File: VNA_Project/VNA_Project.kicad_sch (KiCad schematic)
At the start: 0 parts

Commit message: Started on MCU design, for sweeping
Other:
- added sheet ADC (ADC.kicad_sch)
- added sheet DAC (DAC.kicad_sch)
- added sheet Directional Coupler (Directional_Coupler.kicad_sch)
- added sheet MCU (MCU_vna.kicad_sch)
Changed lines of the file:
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@@
+	)
+	(sheet
+		(at 157.48 38.1)
+		(size 27.94 26.67)
+		(exclude_from_sim no)
+		(in_bom yes)
+		(on_board yes)
+		(dnp no)
+		(fields_autoplaced yes)
+		(stroke
+			(width 0.1524)
+			(type solid)
+		)
+		(fill
+			(color 0 0 0 0.0000)
+		)
+		(property "Sheetname" "Directional Coupler"
+			(at 157.48 37.3884 0)
+			(effects
+				(font
+					(size 1.27 1.27)
+				)
+				(justify left bottom)
+			)
+		)
+		(property "Sheetfile" "Directional_Coupler.kicad_sch"
+			(at 157.48 65.3546 0)
+			(effects
+				(font
+					(size 1.27 1.27)
+				)
+				(justify left top)
+			)
+		)
+		(instances
+			(project "VNA_Project"
+				(path "/8b9c6944-c5f7-4a92-a452-dc4fa5f3924d"
+					(page "5")
+				)
+			)
+		)
+	)
+	(sheet
+		(at 115.57 38.1)
+		(size 26.67 26.67)
+		(exclude_from_sim no)
+		(in_bom yes)
+		(on_board yes)
+		(dnp no)
+		(fields_autoplaced yes)
+		(stroke
+			(width 0.1524)
+			(type solid)
+		)
+		(fill
+			(color 0 0 0 0.0000)
+		)
+		(property "Sheetname" "MCU"
+			(at 115.57 37.3884 0)
+			(effects
+				(font
+					(size 1.27 1.27)
+				)
+				(justify left bottom)
+			)
+		)
+		(property "Sheetfile" "MCU_vna.kicad_sch"
+			(at 115.57 65.3546 0)
+			(effects
+				(font
+					(size 1.27 1.27)
+				)
+				(justify left top)
+			)
+		)
+		(instances
+			(project "VNA_Project"
+				(path "/8b9c6944-c5f7-4a92-a452-dc4fa5f3924d"
+					(page "4")
+				)
+			)
+		)
+	)
+	(sheet
+		(at 76.2 76.2)
+		(size 26.67 22.86)
+		(exclude_from_sim no)
+		(in_bom yes)
+		(on_board yes)
+		(dnp no)
+		(fields_autoplaced yes)
+		(stroke
+			(width 0.1524)
+			(type solid)
+		)
+		(fill
+			(color 0 0 0 0.0000)
+		)
+		(property "Sheetname" "DAC"
+			(at 76.2 75.4884 0)
+			(effects
+				(font
+					(size 1.27 1.27)
+				)
+				(justify left bottom)
+			)
+		)
+		(property "Sheetfile" "DAC.kicad_sch"
+			(at 76.2 99.6446 0)
+			(effects
+				(font
+					(size 1.27 1.27)
+				)
+				(justify left top)
+			)
+		)
+		(instances
+			(project "VNA_Project"
+				(path "/8b9c6944-c5f7-4a92-a452-dc4fa5f3924d"
+					(page "7")
+				)
+			)
+		)
+	)
+	(sheet
+		(at 38.1 77.47)
+		(size 25.4 22.86)
+		(exclude_from_sim no)
+		(in_bom yes)
+		(on_board yes)
+		(dnp no)
+		(fields_autoplaced yes)
+		(stroke
+			(width 0.1524)
+			(type solid)
+		)
+		(fill
+			(color 0 0 0 0.0000)
+		)
+		(property "Sheetname" "ADC"
+			(at 38.1 76.7584 0)
+			(effects
+				(font
+					(size 1.27 1.27)
+				)
+				(justify left bottom)
+			)
+		)
+		(property "Sheetfile" "ADC.kicad_sch"
+			(at 38.1 100.9146 0)
+			(effects
+				(font
+					(size 1.27 1.27)
+				)
+				(justify left top)
+			)
+		)
+		(instances
+			(project "VNA_Project"
+				(path "/8b9c6944-c5f7-4a92-a452-dc4fa5f3924d"
+					(page "6")
+				)
+			)
+		)
 	)
 	(sheet

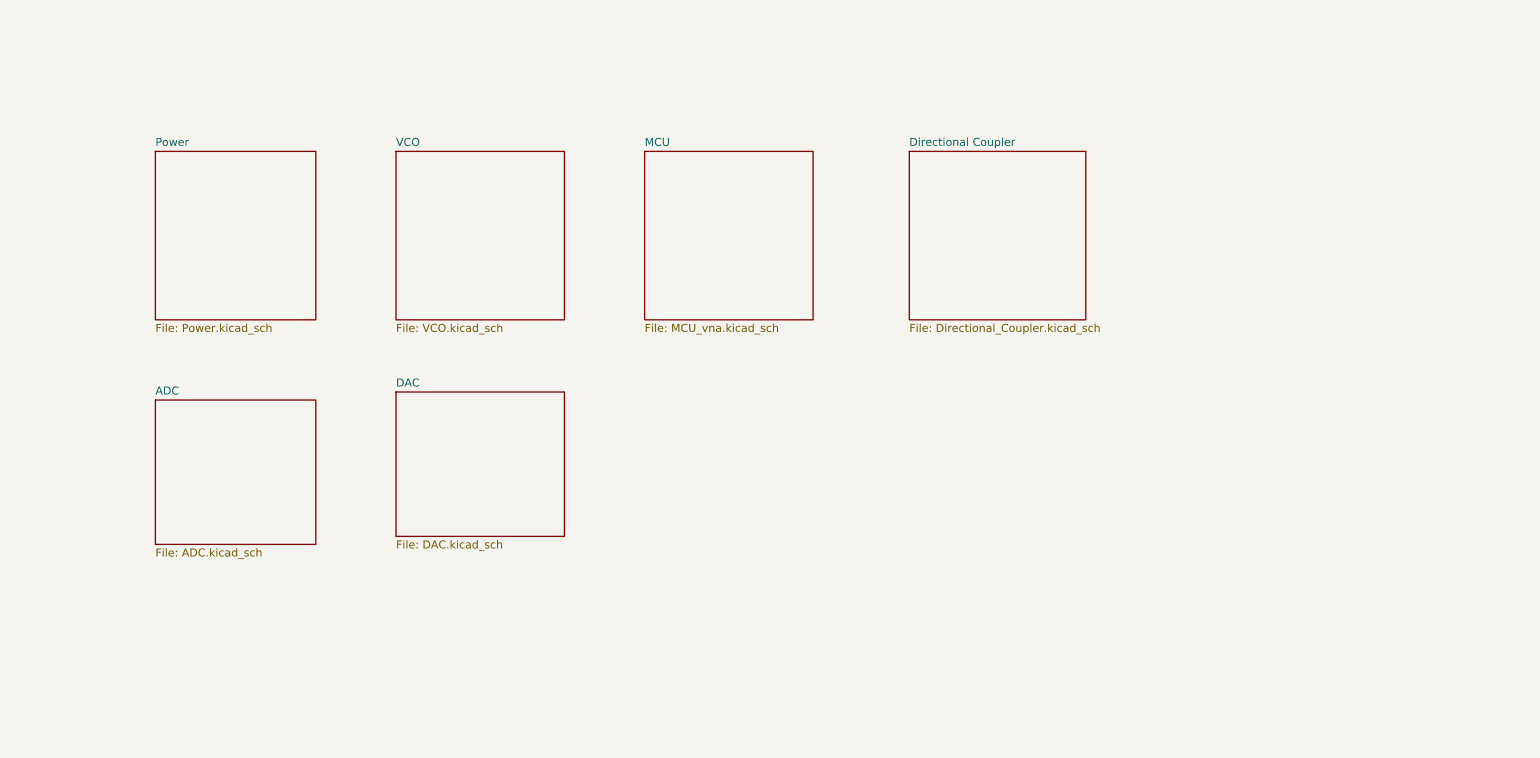
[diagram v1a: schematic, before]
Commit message: Changing from a ESP32 S3 to STM32 H7 high performance MCU for USB HS and ETH capabilities
Changing from a ESP32 S3 to STM32 H7 high performance MCU for USB HS and ETH capabilities
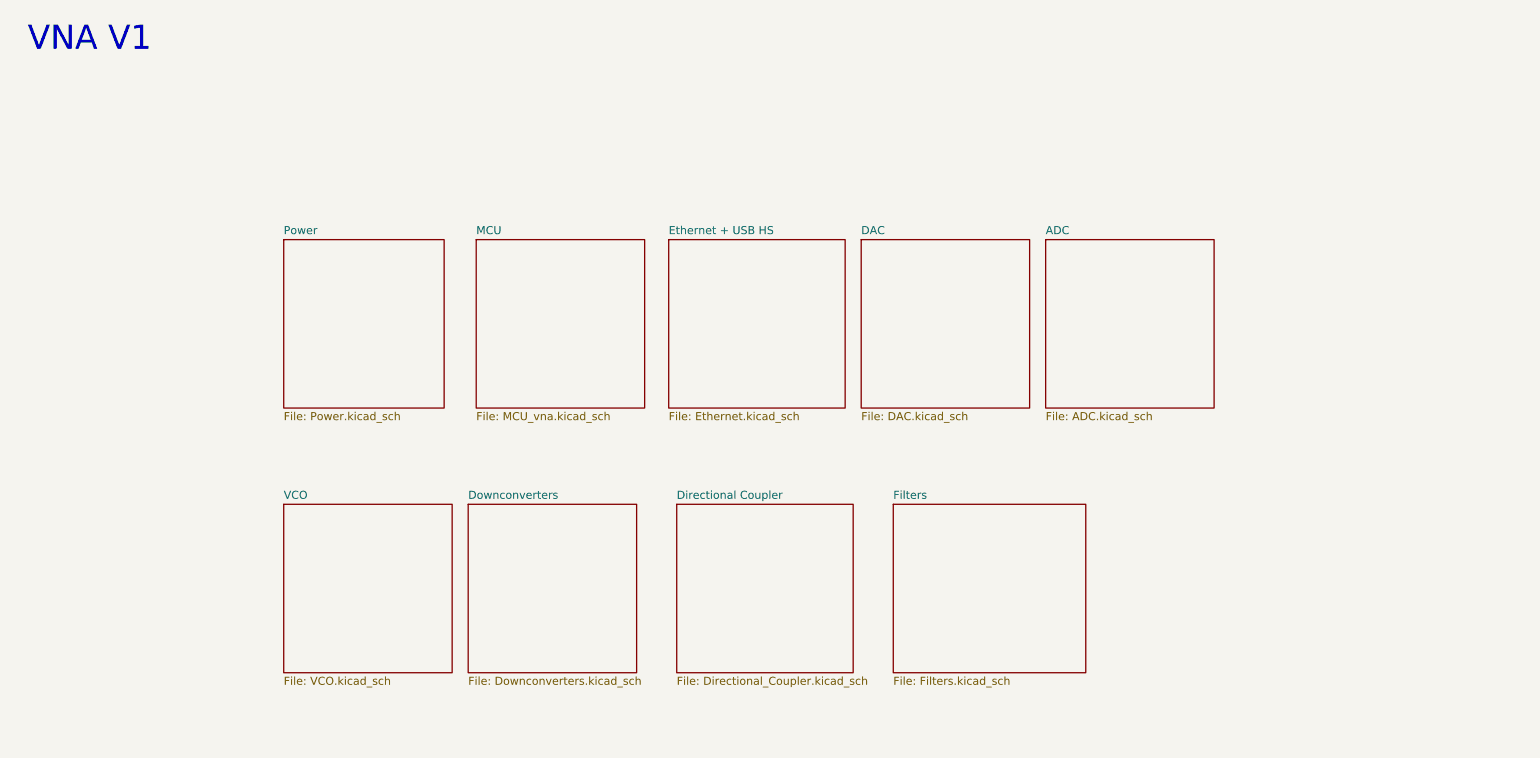
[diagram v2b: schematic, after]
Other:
- added sheet Downconverters (Downconverters.kicad_sch)
- added sheet Ethernet + USB HS (Ethernet.kicad_sch)
- added sheet Filters (Filters.kicad_sch)
- note added: "VNA V1"
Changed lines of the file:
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@@
 	(generator_version "9.0")
 	(paper "A4")
-	(sheet
-		(at 38.1 38.1)
+	(text "VNA V1 "
+		(exclude_from_sim no)
+		(at 27.686 20.32 0)
+		(effects
+			(font
+				(size 3.81 3.81)
+			)
+		)
+	)
+	(sheet
+		(at 58.42 52.07)
 		(size 25.4 26.67)
 		(exclude_from_sim no)
@@
 		)
 		(property "Sheetname" "Power"
-			(at 38.1 37.3884 0)
+			(at 58.42 51.3584 0)
 			(effects
 				(font
@@
 		)
 		(property "Sheetfile" "Power.kicad_sch"
-			(at 38.1 65.3546 0)
+			(at 58.42 79.3246 0)
 			(effects
 				(font
@@
 	)
 	(sheet
-		(at 157.48 38.1)
+		(at 119.38 52.07)
 		(size 27.94 26.67)
 		(exclude_from_sim no)
@@
 			(color 0 0 0 0.0000)
 		)
+		(property "Sheetname" "Ethernet + USB HS"
+			(at 119.38 51.3584 0)
+			(effects
+				(font
+					(size 1.27 1.27)
+				)
+				(justify left bottom)
+			)
+		)
+		(property "Sheetfile" "Ethernet.kicad_sch"
+			(at 119.38 79.3246 0)
+			(effects
+				(font
+					(size 1.27 1.27)
+				)
+				(justify left top)
+			)
+		)
+		(instances
+			(project "VNA_Project"
+				(path "/8b9c6944-c5f7-4a92-a452-dc4fa5f3924d"
+					(page "10")
+				)
+			)
+		)
+	)
+	(sheet
+		(at 120.65 93.98)
+		(size 27.94 26.67)
+		(exclude_from_sim no)
+		(in_bom yes)
+		(on_board yes)
+		(dnp no)
+		(fields_autoplaced yes)
+		(stroke
+			(width 0.1524)
+			(type solid)
+		)
+		(fill
+			(color 0 0 0 0.0000)
+		)
 		(property "Sheetname" "Directional Coupler"
-			(at 157.48 37.3884 0)
+			(at 120.65 93.2684 0)
 			(effects
 				(font
@@
 		)
 		(property "Sheetfile" "Directional_Coupler.kicad_sch"
-			(at 157.48 65.3546 0)
+			(at 120.65 121.2346 0)
 			(effects
 				(font
@@
 	)
 	(sheet
-		(at 115.57 38.1)
+		(at 154.94 93.98)
+		(size 30.48 26.67)
+		(exclude_from_sim no)
+		(in_bom yes)
+		(on_board yes)
+		(dnp no)
+		(fields_autoplaced yes)
+		(stroke
+			(width 0.1524)
+			(type solid)
+		)
+		(fill
+			(color 0 0 0 0.0000)
+		)
+		(property "Sheetname" "Filters"
+			(at 154.94 93.2684 0)
+			(effects
+				(font
+					(size 1.27 1.27)
+				)
+				(justify left bottom)
+			)
+		)
+		(property "Sheetfile" "Filters.kicad_sch"
+			(at 154.94 121.2346 0)
+			(effects
+				(font
+					(size 1.27 1.27)
+				)
+				(justify left top)
+			)
+		)
+		(instances
+			(project "VNA_Project"
+				(path "/8b9c6944-c5f7-4a92-a452-dc4fa5f3924d"
+					(page "9")
+				)
+			)
+		)
+	)
+	(sheet
+		(at 88.9 52.07)
 		(size 26.67 26.67)
 		(exclude_from_sim no)
@@
 		)
 		(property "Sheetname" "MCU"
-			(at 115.57 37.3884 0)
+			(at 88.9 51.3584 0)
 			(effects
 				(font
@@
 		)
 		(property "Sheetfile" "MCU_vna.kicad_sch"
-			(at 115.57 65.3546 0)
+			(at 88.9 79.3246 0)
 			(effects
 				(font
@@
 	)
 	(sheet
-		(at 76.2 76.2)
-		(size 26.67 22.86)
+		(at 149.86 52.07)
+		(size 26.67 26.67)
 		(exclude_from_sim no)
 		(in_bom yes)
@@
 		)
 		(property "Sheetname" "DAC"
-			(at 76.2 75.4884 0)
+			(at 149.86 51.3584 0)
 			(effects
 				(font
@@
 		)
 		(property "Sheetfile" "DAC.kicad_sch"
-			(at 76.2 99.6446 0)
+			(at 149.86 79.3246 0)
 			(effects
 				(font
@@
 	)
 	(sheet
-		(at 38.1 77.47)
-		(size 25.4 22.86)
+		(at 179.07 52.07)
+		(size 26.67 26.67)
 		(exclude_from_sim no)
 		(in_bom yes)
@@
 		)
 		(property "Sheetname" "ADC"
-			(at 38.1 76.7584 0)
+			(at 179.07 51.3584 0)
 			(effects
 				(font
@@
 		)
 		(property "Sheetfile" "ADC.kicad_sch"
-			(at 38.1 100.9146 0)
+			(at 179.07 79.3246 0)
 			(effects
 				(font
@@
 	)
 	(sheet
-		(at 76.2 38.1)
+		(at 58.42 93.98)
 		(size 26.67 26.67)
 		(exclude_from_sim no)
@@
 		)
 		(property "Sheetname" "VCO"
-			(at 76.2 37.3884 0)
+			(at 58.42 93.2684 0)
 			(effects
 				(font
@@
 		)
 		(property "Sheetfile" "VCO.kicad_sch"
-			(at 76.2 65.3546 0)
+			(at 58.42 121.2346 0)
 			(effects
 				(font
@@
 				)
 			)
+		)
+	)
+	(sheet
+		(at 87.63 93.98)
+		(size 26.67 26.67)
+		(exclude_from_sim no)
+		(in_bom yes)
+		(on_board yes)
+		(dnp no)
+		(fields_autoplaced yes)
+		(stroke
+			(width 0.1524)
+			(type solid)
+		)
+		(fill
+			(color 0 0 0 0.0000)
+		)
+		(property "Sheetname" "Downconverters"
+			(at 87.63 93.2684 0)
+			(effects
+				(font
+					(size 1.27 1.27)
+				)
+				(justify left bottom)
+			)
+		)
+		(property "Sheetfile" "Downconverters.kicad_sch"
+			(at 87.63 121.2346 0)
+			(effects
+				(font
+					(size 1.27 1.27)
+				)
+				(justify left top)
+			)
+		)
+		(instances
+			(project "VNA_Project"
+				(path "/8b9c6944-c5f7-4a92-a452-dc4fa5f3924d"
+					(page "8")
+				)
+			)

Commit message: minor changes
minor changes
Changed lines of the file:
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@@
 	)
 	(sheet
-		(at 120.65 93.98)
+		(at 135.89 91.44)
 		(size 27.94 26.67)
 		(exclude_from_sim no)
@@
 		)
 		(property "Sheetname" "Directional Coupler"
-			(at 120.65 93.2684 0)
+			(at 135.89 90.7284 0)
 			(effects
 				(font
@@
 		)
 		(property "Sheetfile" "Directional_Coupler.kicad_sch"
-			(at 120.65 121.2346 0)
+			(at 135.89 118.6946 0)
 			(effects
 				(font
@@
 	)
 	(sheet
-		(at 154.94 93.98)
-		(size 30.48 26.67)
+		(at 175.26 91.44)
+		(size 27.94 26.67)
 		(exclude_from_sim no)
 		(in_bom yes)
@@
 		)
 		(property "Sheetname" "Filters"
-			(at 154.94 93.2684 0)
+			(at 175.26 90.7284 0)
 			(effects
 				(font
@@
 		)
 		(property "Sheetfile" "Filters.kicad_sch"
-			(at 154.94 121.2346 0)
+			(at 175.26 118.6946 0)
 			(effects
 				(font
@@
 	)
 	(sheet
-		(at 58.42 93.98)
-		(size 26.67 26.67)
+		(at 58.42 91.44)
+		(size 27.94 26.67)
 		(exclude_from_sim no)
 		(in_bom yes)
@@
 		)
 		(property "Sheetname" "VCO"
-			(at 58.42 93.2684 0)
+			(at 58.42 90.7284 0)
 			(effects
 				(font
@@
 		)
 		(property "Sheetfile" "VCO.kicad_sch"
-			(at 58.42 121.2346 0)
+			(at 58.42 118.6946 0)
 			(effects
 				(font
@@
 	)
 	(sheet
-		(at 87.63 93.98)
-		(size 26.67 26.67)
+		(at 97.79 91.44)
+		(size 27.94 26.67)
 		(exclude_from_sim no)
 		(in_bom yes)
@@
 		)
 		(property "Sheetname" "Downconverters"
-			(at 87.63 93.2684 0)
+			(at 97.79 90.7284 0)
 			(effects
 				(font
@@
 		)
 		(property "Sheetfile" "Downconverters.kicad_sch"
-			(at 87.63 121.2346 0)
-			(effects
-				(font
+			(at 97.79 118.6946 0)
+			(effects
+				(font

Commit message: Eth done
Eth done
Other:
- sheet Ethernet + USB HS renamed Ethernet
- added sheet USB HS (USB_HS.kicad_sch)
- company: (none) -> Flatrim Dreshaj
- title: (none) -> VNA V1 
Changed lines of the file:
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@@
 	(generator_version "9.0")
 	(paper "A4")
+	(title_block
+		(title "VNA V1 ")
+		(company "Flatrim Dreshaj")
+	)
 	(text "VNA V1 "
 		(exclude_from_sim no)
@@
 			(color 0 0 0 0.0000)
 		)
-		(property "Sheetname" "Ethernet + USB HS"
+		(property "Sheetname" "Ethernet"
 			(at 119.38 51.3584 0)
 			(effects
@@
 	)
 	(sheet
-		(at 149.86 52.07)
+		(at 152.4 52.07)
+		(size 27.94 26.67)
+		(exclude_from_sim no)
+		(in_bom yes)
+		(on_board yes)
+		(dnp no)
+		(fields_autoplaced yes)
+		(stroke
+			(width 0.1524)
+			(type solid)
+		)
+		(fill
+			(color 0 0 0 0.0000)
+		)
+		(property "Sheetname" "USB HS"
+			(at 152.4 51.3584 0)
+			(effects
+				(font
+					(size 1.27 1.27)
+				)
+				(justify left bottom)
+			)
+		)
+		(property "Sheetfile" "USB_HS.kicad_sch"
+			(at 152.4 79.3246 0)
+			(effects
+				(font
+					(size 1.27 1.27)
+				)
+				(justify left top)
+			)
+		)
+		(instances
+			(project "VNA_Project"
+				(path "/8b9c6944-c5f7-4a92-a452-dc4fa5f3924d"
+					(page "11")
+				)
+			)
+		)
+	)
+	(sheet
+		(at 190.5 52.07)
 		(size 26.67 26.67)
 		(exclude_from_sim no)
@@
 		)
 		(property "Sheetname" "DAC"
-			(at 149.86 51.3584 0)
+			(at 190.5 51.3584 0)
 			(effects
 				(font
@@
 		)
 		(property "Sheetfile" "DAC.kicad_sch"
-			(at 149.86 79.3246 0)
+			(at 190.5 79.3246 0)
 			(effects
 				(font
@@
 	)
 	(sheet
-		(at 179.07 52.07)
+		(at 228.6 52.07)
 		(size 26.67 26.67)
 		(exclude_from_sim no)
@@
 		)
 		(property "Sheetname" "ADC"
-			(at 179.07 51.3584 0)
+			(at 228.6 51.3584 0)
 			(effects
 				(font
@@
 		)
 		(property "Sheetfile" "ADC.kicad_sch"
-			(at 179.07 79.3246 0)
-			(effects
-				(font
+			(at 228.6 79.3246 0)
+			(effects
+				(font

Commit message: minor changes
minor changes
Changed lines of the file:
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@@
 	(sheet
 		(at 58.42 91.44)
-		(size 27.94 26.67)
+		(size 27.94 25.4)
 		(exclude_from_sim no)
 		(in_bom yes)
@@
 		)
 		(property "Sheetfile" "VCO.kicad_sch"
-			(at 58.42 118.6946 0)
+			(at 58.42 117.4246 0)
 			(effects
 				(font

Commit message: adc
adc
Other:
- removed sheet USB HS
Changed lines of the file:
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@@
 	)
 	(sheet
-		(at 58.42 52.07)
+		(at 68.58 66.04)
 		(size 25.4 26.67)
 		(exclude_from_sim no)
@@
 		)
 		(property "Sheetname" "Power"
-			(at 58.42 51.3584 0)
+			(at 68.58 65.3284 0)
 			(effects
 				(font
@@
 		)
 		(property "Sheetfile" "Power.kicad_sch"
-			(at 58.42 79.3246 0)
+			(at 68.58 93.2946 0)
 			(effects
 				(font
@@
 	)
 	(sheet
-		(at 119.38 52.07)
-		(size 27.94 26.67)
+		(at 129.54 66.04)
+		(size 26.67 26.67)
 		(exclude_from_sim no)
 		(in_bom yes)
@@
 		)
 		(property "Sheetname" "Ethernet"
-			(at 119.38 51.3584 0)
+			(at 129.54 65.3284 0)
 			(effects
 				(font
@@
 		)
 		(property "Sheetfile" "Ethernet.kicad_sch"
-			(at 119.38 79.3246 0)
+			(at 129.54 93.2946 0)
 			(effects
 				(font
@@
 	)
 	(sheet
-		(at 135.89 91.44)
-		(size 27.94 26.67)
+		(at 144.78 104.14)
+		(size 25.4 25.4)
 		(exclude_from_sim no)
 		(in_bom yes)
@@
 		)
 		(property "Sheetname" "Directional Coupler"
-			(at 135.89 90.7284 0)
+			(at 144.78 103.4284 0)
 			(effects
 				(font
@@
 		)
 		(property "Sheetfile" "Directional_Coupler.kicad_sch"
-			(at 135.89 118.6946 0)
+			(at 144.78 130.1246 0)
 			(effects
 				(font
@@
 	)
 	(sheet
-		(at 175.26 91.44)
-		(size 27.94 26.67)
+		(at 181.61 104.14)
+		(size 25.4 25.4)
 		(exclude_from_sim no)
 		(in_bom yes)
@@
 		)
 		(property "Sheetname" "Filters"
-			(at 175.26 90.7284 0)
+			(at 181.61 103.4284 0)
 			(effects
 				(font
@@
 		)
 		(property "Sheetfile" "Filters.kicad_sch"
-			(at 175.26 118.6946 0)
+			(at 181.61 130.1246 0)
 			(effects
 				(font
@@
 	)
 	(sheet
-		(at 88.9 52.07)
+		(at 99.06 66.04)
+		(size 25.4 26.67)
+		(exclude_from_sim no)
+		(in_bom yes)
+		(on_board yes)
+		(dnp no)
+		(fields_autoplaced yes)
+		(stroke
+			(width 0.1524)
+			(type solid)
+		)
+		(fill
+			(color 0 0 0 0.0000)
+		)
+		(property "Sheetname" "MCU"
+			(at 99.06 65.3284 0)
+			(effects
+				(font
+					(size 1.27 1.27)
+				)
+				(justify left bottom)
+			)
+		)
+		(property "Sheetfile" "MCU_vna.kicad_sch"
+			(at 99.06 93.2946 0)
+			(effects
+				(font
+					(size 1.27 1.27)
+				)
+				(justify left top)
+			)
+		)
+		(instances
+			(project "VNA_Project"
+				(path "/8b9c6944-c5f7-4a92-a452-dc4fa5f3924d"
+					(page "4")
+				)
+			)
+		)
+	)
+	(sheet
+		(at 160.02 66.04)
 		(size 26.67 26.67)
 		(exclude_from_sim no)
@@
 			(color 0 0 0 0.0000)
 		)
-		(property "Sheetname" "MCU"
-			(at 88.9 51.3584 0)
-			(effects
-				(font
-					(size 1.27 1.27)
-				)
-				(justify left bottom)
-			)
-		)
-		(property "Sheetfile" "MCU_vna.kicad_sch"
-			(at 88.9 79.3246 0)
-			(effects
-				(font
-					(size 1.27 1.27)
-				)
-				(justify left top)
-			)
-		)
-		(instances
-			(project "VNA_Project"
-				(path "/8b9c6944-c5f7-4a92-a452-dc4fa5f3924d"
-					(page "4")
-				)
-			)
-		)
-	)
-	(sheet
-		(at 152.4 52.07)
-		(size 27.94 26.67)
-		(exclude_from_sim no)
-		(in_bom yes)
-		(on_board yes)
-		(dnp no)
-		(fields_autoplaced yes)
-		(stroke
-			(width 0.1524)
-			(type solid)
-		)
-		(fill
-			(color 0 0 0 0.0000)
-		)
-		(property "Sheetname" "USB HS"
-			(at 152.4 51.3584 0)
-			(effects
-				(font
-					(size 1.27 1.27)
-				)
-				(justify left bottom)
-			)
-		)
-		(property "Sheetfile" "USB_HS.kicad_sch"
-			(at 152.4 79.3246 0)
-			(effects
-				(font
-					(size 1.27 1.27)
-				)
-				(justify left top)
-			)
-		)
-		(instances
-			(project "VNA_Project"
-				(path "/8b9c6944-c5f7-4a92-a452-dc4fa5f3924d"
-					(page "11")
-				)
-			)
-		)
-	)
-	(sheet
-		(at 190.5 52.07)
+		(property "Sheetname" "DAC"
+			(at 160.02 65.3284 0)
+			(effects
+				(font
+					(size 1.27 1.27)
+				)
+				(justify left bottom)
+			)
+		)
+		(property "Sheetfile" "DAC.kicad_sch"
+			(at 160.02 93.2946 0)
+			(effects
+				(font
+					(size 1.27 1.27)
+				)
+				(justify left top)
+			)
+		)
+		(instances
+			(project "VNA_Project"
+				(path "/8b9c6944-c5f7-4a92-a452-dc4fa5f3924d"
+					(page "7")
+				)
+			)
+		)
+	)
+	(sheet
+		(at 189.23 66.04)
 		(size 26.67 26.67)
 		(exclude_from_sim no)
@@
 			(color 0 0 0 0.0000)
 		)
-		(property "Sheetname" "DAC"
-			(at 190.5 51.3584 0)
-			(effects
-				(font
-					(size 1.27 1.27)
-				)
-				(justify left bottom)
-			)
-		)
-		(property "Sheetfile" "DAC.kicad_sch"
-			(at 190.5 79.3246 0)
-			(effects
-				(font
-					(size 1.27 1.27)
-				)
-				(justify left top)
-			)
-		)
-		(instances
-			(project "VNA_Project"
-				(path "/8b9c6944-c5f7-4a92-a452-dc4fa5f3924d"
-					(page "7")
-				)
-			)
-		)
-	)
-	(sheet
-		(at 228.6 52.07)
-		(size 26.67 26.67)
-		(exclude_from_sim no)
-		(in_bom yes)
-		(on_board yes)
-		(dnp no)
-		(fields_autoplaced yes)
-		(stroke
-			(width 0.1524)
-			(type solid)
-		)
-		(fill
-			(color 0 0 0 0.0000)
-		)
 		(property "Sheetname" "ADC"
-			(at 228.6 51.3584 0)
+			(at 189.23 65.3284 0)
 			(effects
 				(font
@@
 		)
 		(property "Sheetfile" "ADC.kicad_sch"
-			(at 228.6 79.3246 0)
+			(at 189.23 93.2946 0)
 			(effects
 				(font
@@
 	)
 	(sheet
-		(at 58.42 91.44)
-		(size 27.94 25.4)
+		(at 76.2 104.14)
+		(size 25.4 25.4)
 		(exclude_from_sim no)
 		(in_bom yes)
@@
 		)
 		(property "Sheetname" "VCO"
-			(at 58.42 90.7284 0)
+			(at 76.2 103.4284 0)
 			(effects
 				(font
@@
 		)
 		(property "Sheetfile" "VCO.kicad_sch"
-			(at 58.42 117.4246 0)
+			(at 76.2 130.1246 0)
 			(effects
 				(font
@@
 	)
 	(sheet
-		(at 97.79 91.44)
-		(size 27.94 26.67)
+		(at 107.95 104.14)
+		(size 25.4 25.4)
 		(exclude_from_sim no)
 		(in_bom yes)
@@
 		)
 		(property "Sheetname" "Downconverters"
-			(at 97.79 90.7284 0)
+			(at 107.95 103.4284 0)
 			(effects
 				(font
@@
 		)
 		(property "Sheetfile" "Downconverters.kicad_sch"
-			(at 97.79 118.6946 0)
-			(effects
-				(font
+			(at 107.95 130.1246 0)
+			(effects
+				(font
